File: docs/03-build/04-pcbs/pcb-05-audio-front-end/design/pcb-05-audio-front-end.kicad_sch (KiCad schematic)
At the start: 55 parts, among them J1 J5-1 host (W26), J2 J5-2 REAR_L, J3 J5-3 FRONT_L, J4 J5-4 REAR_R, J5 J5-5 FRONT_R, J6 J5-6 speaker (W28), J7 J5-7 +5 V (W12), U1 ADAU7002ACBZ-R7, U2 ADAU7002ACBZ-R7, U3 MAX98357AETE+T

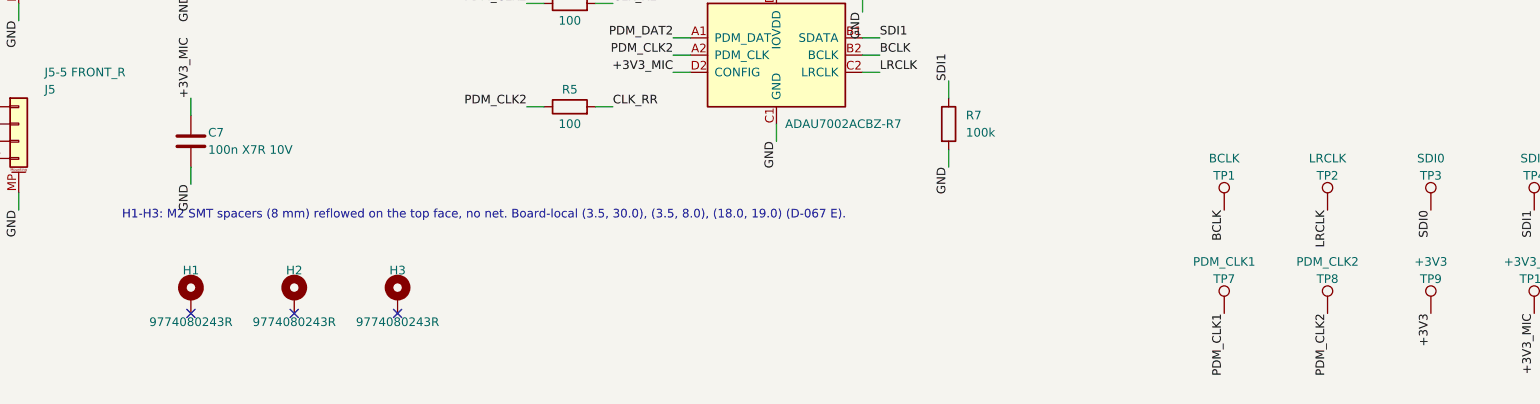
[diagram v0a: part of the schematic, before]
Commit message: build(pcbs): PCB-05 board set-up with envelope keep-outs; J7 tails clipped, plated spacer holes (D-067 amended, lesson 3)
30 x 38 x 1.6 mm two-layer outline with origins at board-local (0, 0);
fab-neutral rules plus a 0.5 mm minimum on the amp's 5 V and speaker
tracks; rule areas for a bare bottom face and for no pins over the Pi's
USB jacks 2.10 mm below; the envelope on user layers (connectors, what is
below, frame bosses, ceilings). All rules proven on a scratch copy.

Set-up found J5-7's through-hole tails and peg about 0.5 mm above a USB
jack, and Wurth's spacer land pattern with copper at its own hole's edge.
Builder chose H1 (keep the 43650-0200, clip tails to <= 0.5 mm and the peg
flush; rule area notched at J7) and I1 (spacer holes plated, project
footprint from Wurth's). ADAU7002 footprint allows its shared mask opening.
Empty board DRC 0; ERC still 0/0.

Co-Authored-By: Claude Opus 5.5 <noreply@anthropic.com>
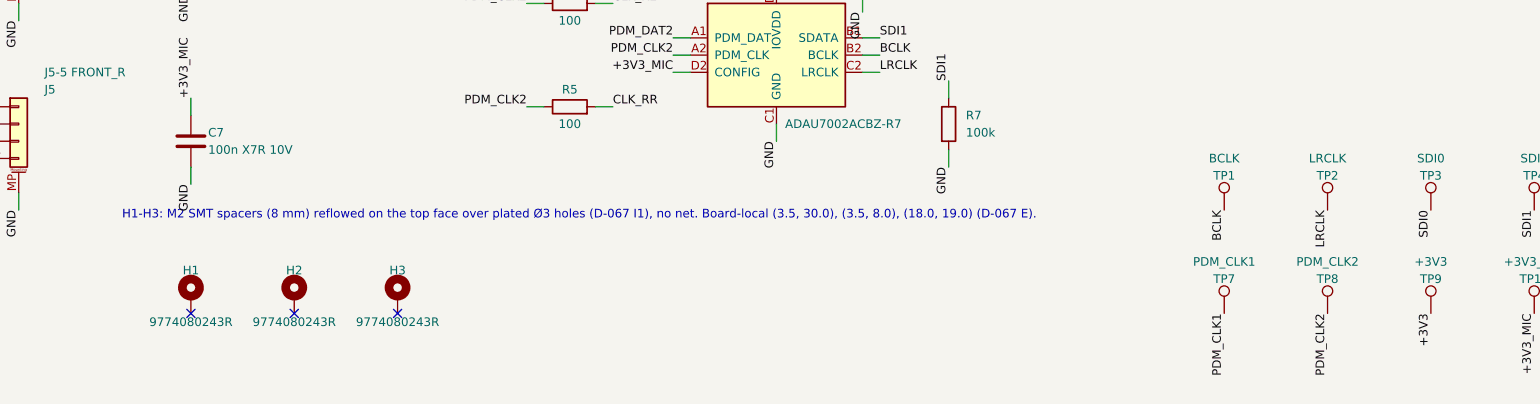
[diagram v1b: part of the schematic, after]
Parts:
- H1, H2, H3: footprint Mounting_Wuerth:Mounting_Wuerth_WA-SMSI-M2_H8mm_9774080243 -> pcb05:Wurth_WA-SMSI-M2_H8mm_9774080243_PTH
- J7: Assembly (none) -> After soldering, clip both tails to <= 0.5 mm below the boa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
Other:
- note added: "H1-H3: M2 SMT spacers (8 mm) reflowed on the top face over plated Ø3 holes (D-067 I1), no net. Board-local (3.5, 30.0), (3.5, 8.0), (18.0, 19.0) (D-067 E)."
- note removed: "H1-H3: M2 SMT spacers (8 mm) reflowed on the top face, no net. Board-local (3.5, 30.0), (3.5, 8.0), (18.0, 19.0) (D-067 E)."

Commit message: build(pcbs): PCB-05 placed and routed on 4 layers, DRC clean (D-067 amended, lesson 4)
Placement found the lesson-1 fixing on the GH pads (J1: one rear, two front
spacers; J5-1 2 mm toward -Y; J5-7 at its real 9.65 mm width; mount check 7/7).
Routing the left half needed 4 layers (L2: In1 solid GND, In2 GND + slow rows,
B.Cu clock bus) and a J5-1 reorder (LRCLK above BCLK; SDI1 above SDI0).
DRC 0 errors, 0 unconnected, parity clean; 30 cosmetic lib_footprint_mismatch.
kp.py: library_models() reads one-line (model ...) entries (U1/U2 had lost
their models); remove_in() helper. Playbook: four more PCB-05 traps.

Co-Authored-By: Claude Opus 5.5 <noreply@anthropic.com>
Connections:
- net BCLK: now also J1.4 (Pin_4); no longer J1.3 (Pin_3)
- net GND: now also J1.3 (Pin_3), J1.5 (Pin_5); no longer J1.2 (Pin_2), J1.4 (Pin_4)
- net LRCLK: now also J1.2 (Pin_2); no longer J1.5 (Pin_5)
- net SDI0: now also J1.8 (Pin_8); no longer J1.7 (Pin_7)
- net SDI1: now also J1.7 (Pin_7); no longer J1.8 (Pin_8)

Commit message: build(pcbs): PCB-05 audio front end rev A; fit check passes (lesson 5)
Board STEP with every part: U3's TQFN and J7's Micro-Fit named models KiCad
doesn't ship, so both use project footprint copies (J7's model from Molex's
dimensions, tails clipped per D-067 H1). Fab outputs in fab/revA: 4-layer
Gerbers, drill, BOM, placement and JLCPCB CPL from the board-local origin, zip
and order parameters. check_pcb05_fit.py places the STEP in the droid: 8/8
(J7 housing 0.98 under the front boss, clipped tails 1.63 above the Pi's USB
jack, install slide 0.46). kp.audit() now checks model files exist.

Co-Authored-By: Claude Opus 5.5 <noreply@anthropic.com>
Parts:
- J7: footprint Connector_Molex:Molex_Micro-Fit_3.0_43650-0200_1x02_P3.00mm_Horizontal -> pcb05:Molex_Micro-Fit_3.0_43650-0200_1x02_P3.00mm_Horizontal
- U3: footprint Package_DFN_QFN:TQFN-16-1EP_3x3mm_P0.5mm_EP1.23x1.23mm -> pcb05:TQFN-16-1EP_3x3mm_P0.5mm_EP1.23x1.23mm
